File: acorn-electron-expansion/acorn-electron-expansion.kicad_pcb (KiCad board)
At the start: 2 copper layers, 100 x 100 mm, 11 parts, among them P1 Acorn Electron Expansion Conn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, P2 CONN_02X24, U1 74hct125d, U2 74LVC245 D0-7, U3 74LVC245 A0-7, U4 74LVC245 A8-15, U5 74LVC245

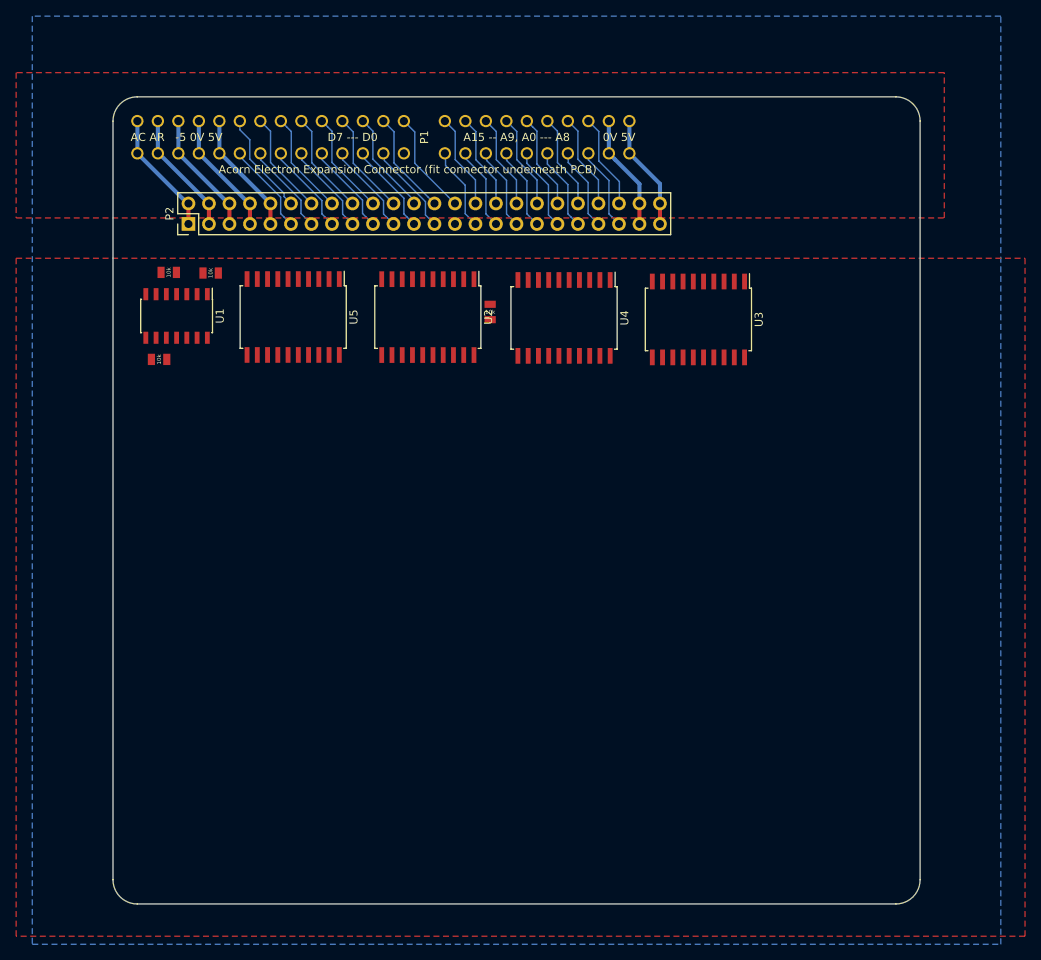
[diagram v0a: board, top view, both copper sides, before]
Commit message: Made library and module for Scarab miniSpartan6+ board, and routed most of the level conversion stuff up top
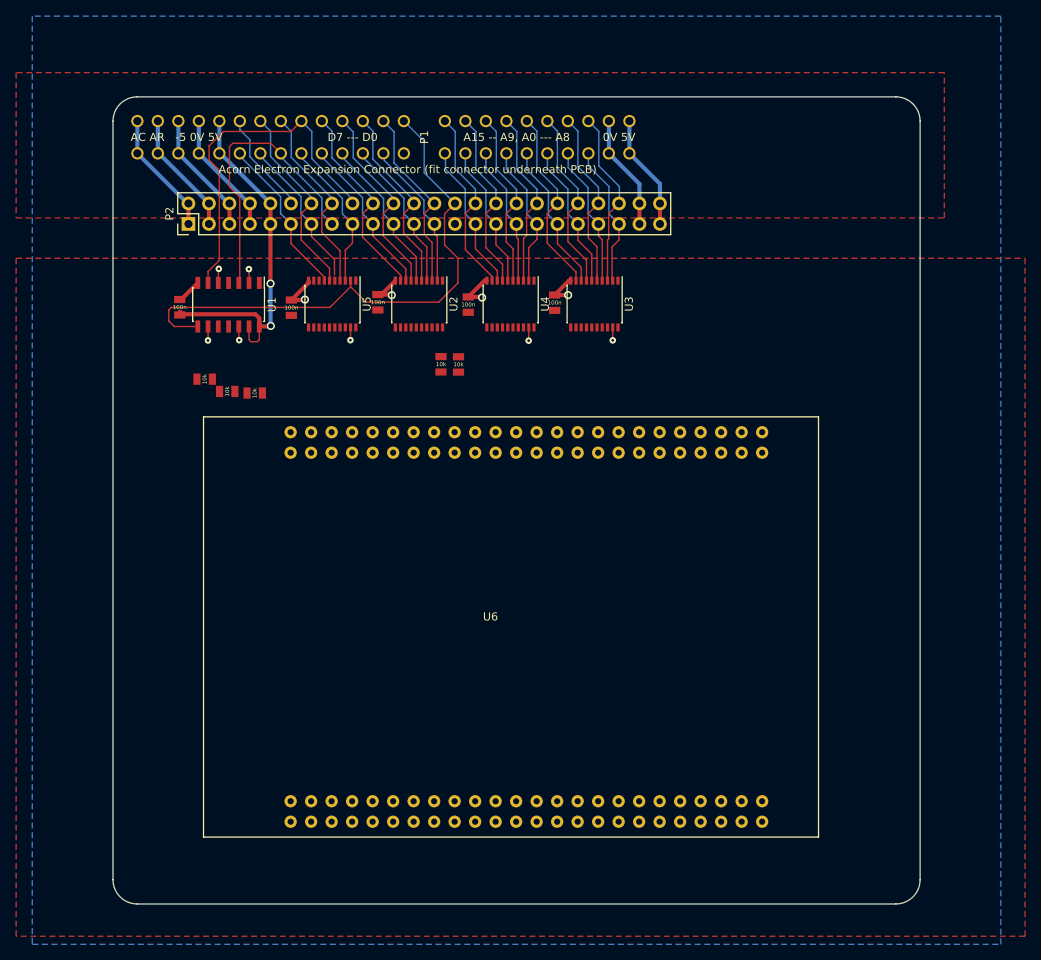
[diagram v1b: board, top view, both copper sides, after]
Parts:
- added C1: 100n, myelin-kicad:C0805_nosilkscreen, F.Cu at (108.3, 76.1)
- added C2: 100n, myelin-kicad:C0805_nosilkscreen, F.Cu at (122.1, 76.1)
- added C3: 100n, myelin-kicad:C0805_nosilkscreen, F.Cu at (132.8, 75.5)
- added C4: 100n, myelin-kicad:C0805_nosilkscreen, F.Cu at (144.0, 75.7)
- added C5: 100n, myelin-kicad:C0805_nosilkscreen, F.Cu at (154.7, 75.5)
- added R5: 10k, myelin-kicad:R0805_nosilkscreen, F.Cu at (140.6, 83.1)
- added U6: scarab_mini_spartan_6_lx25, myelin-kicad:scarab_mini_spartan_6_lx25, F.Cu at (111.2, 141.1)
- U2, U3, U4, U5: footprint Housings_SOIC:SOIC-20W_7.5x12.8mm_Pitch1.27mm -> Housings_SSOP:SSOP-20_4.4x6.5mm_Pitch0.65mm
- moved R1 15.8 mm to (117.6, 86.7)
- moved R2 14.0 mm to (111.4, 85.0)
- moved U3 13.0 mm to (159.6, 75.7)
- moved R3 9.33 mm to (114.2, 86.5)
- moved R4 7.59 mm to (142.8, 83.2)
- moved U4 6.86 mm to (149.2, 75.7)
- moved U1 6.59 mm to (114.3, 75.8)
- moved U5 5.10 mm to (127.2, 75.7)
- moved U2 1.96 mm to (137.9, 75.7)
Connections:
- U1 pad 13: Net-(U1-Pad13) -> /5V
- U2 pad 19: /GND -> /DATA_nOE
- U5 pad 13: /nRDY_3V -> /16MHZ_3V
- U5 pad 14: /16MHZ_3V -> /PHI0_3V
- U5 pad 15: /PHI0_3V -> /nRST_3V
- U5 pad 16: /nRST_3V -> /16MHZ_DIV13_3V
- U5 pad 17: /16MHZ_DIV13_3V -> /RnW_3V
- U5 pad 18: /RnW_3V -> /nRDY_3V
- U5 pad 2: /RnW -> /nRDY
- U5 pad 3: /16MHZ_DIV13 -> /RnW
- U5 pad 4: /nRST -> /16MHZ_DIV13
- U5 pad 6: /16MHZ -> /nRST
- U5 pad 7: /nRDY -> /16MHZ
- U5 pad 8: Net-(U5-Pad8) -> /GND
- U5 pad 9: Net-(U5-Pad9) -> /GND
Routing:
- net /nRDY: track 12.8 -> 68.6 mm
- net /GND: track 29.8 -> 64.0 mm, vias 0 -> 11
- net /nIRQ: track 12.8 -> 43.6 mm
- net /5V: track 29.8 -> 59.8 mm, vias 0 -> 2
- net /nNMI: track 11.4 -> 36.3 mm
- net /D7: track 12.8 -> 25.0 mm
- net /nRST: track 12.8 -> 24.5 mm
- net /D5: track 12.8 -> 24.4 mm
- net /A1: track 11.8 -> 23.3 mm
- net /A15: track 11.8 -> 23.2 mm
- net /16MHZ_DIV13: track 12.8 -> 23.9 mm
- net /D3: track 12.8 -> 23.9 mm
- net /A3: track 11.8 -> 22.8 mm
- net /A13: track 11.8 -> 22.7 mm
- net /D1: track 12.8 -> 23.4 mm
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
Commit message: Possibly final board... needs verification but almost ready to go to fab
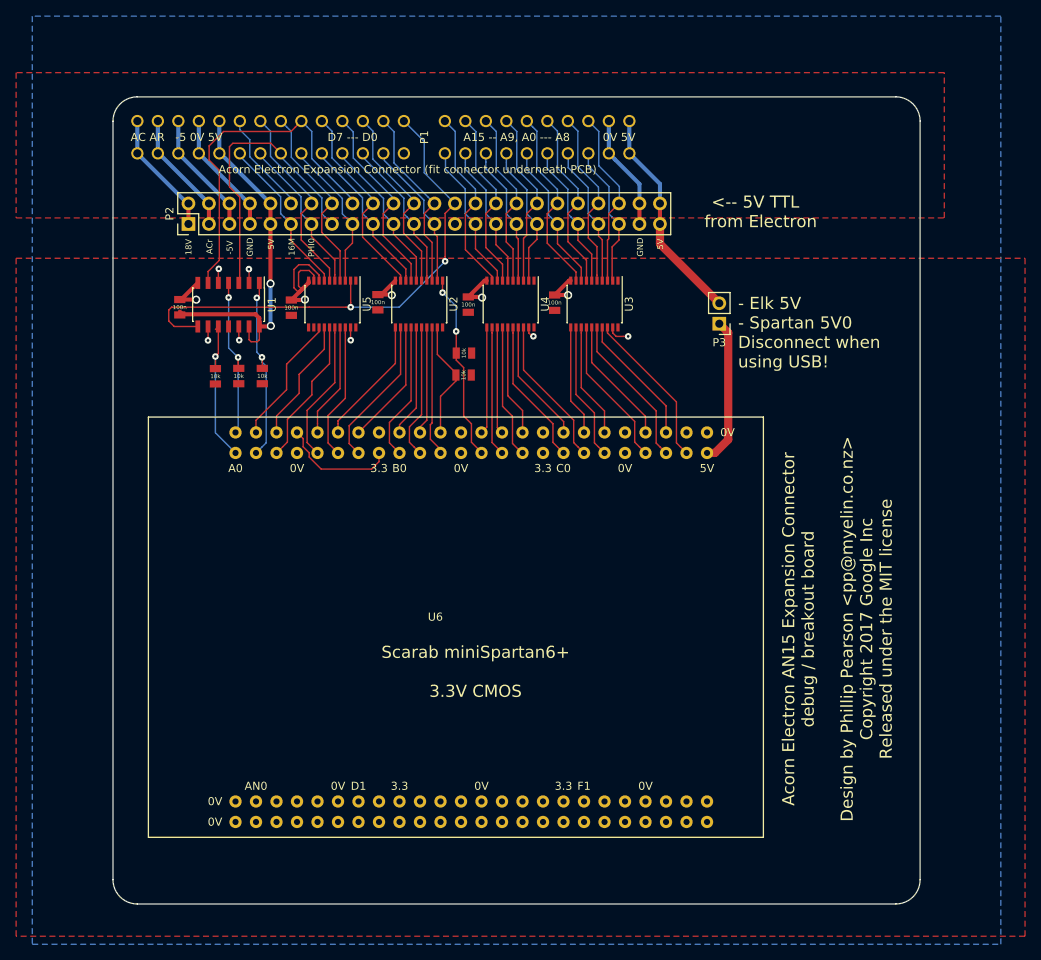
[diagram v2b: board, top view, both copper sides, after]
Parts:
- added P3: 5V / 5V0, Pin_Headers:Pin_Header_Straight_1x02_Pitch2.54mm, F.Cu at (175.1, 78.1)
- moved U6 6.83 mm to (104.4, 141.1)
- moved R2 4.24 mm to (115.6, 84.6), turned to 90 degrees
- moved R5 3.11 mm to (143.4, 84.5), turned to 180 degrees
- moved R3 2.38 mm to (112.7, 84.6), turned to 270 degrees
- moved R1 2.31 mm to (118.5, 84.6), turned to 90 degrees
- moved R4 1.56 mm to (143.5, 81.8), turned to 180 degrees
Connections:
- U6 pad A0: Net-(U6-PadA0) -> /nASSERT_nRDY
- U6 pad A1: (no net) -> /nASSERT_nIRQ
- U6 pad A10: Net-(U6-PadA10) -> /D6_3V
- U6 pad A11: Net-(U6-PadA11) -> /D5_3V
- U6 pad A2: Net-(U6-PadA2) -> /nASSERT_nNMI
- U6 pad A3: Net-(U6-PadA3) -> /16MHZ_3V
- U6 pad A4: Net-(U6-PadA4) -> /nRST_3V
- U6 pad A5: Net-(U6-PadA5) -> /PHI0_3V
- U6 pad A6: Net-(U6-PadA6) -> /16MHZ_DIV13_3V
- U6 pad A7: Net-(U6-PadA7) -> /RnW_3V
- U6 pad A8: Net-(U6-PadA8) -> /nRDY_3V
- U6 pad A9: Net-(U6-PadA9) -> /D7_3V
- U6 pad B0: Net-(U6-PadB0) -> /D4_3V
- U6 pad B1: Net-(U6-PadB1) -> /D3_3V
- U6 pad B10: Net-(U6-PadB10) -> /A12_3V
- U6 pad B11: Net-(U6-PadB11) -> /A11_3V
- U6 pad B2: Net-(U6-PadB2) -> /D2_3V
- U6 pad B3: Net-(U6-PadB3) -> /D1_3V
- U6 pad B4: Net-(U6-PadB4) -> /D0_3V
- U6 pad B5: Net-(U6-PadB5) -> /DATA_nOE
- U6 pad B6: Net-(U6-PadB6) -> /DATA_READ
- U6 pad B7: Net-(U6-PadB7) -> /A15_3V
- U6 pad B8: Net-(U6-PadB8) -> /A14_3V
- U6 pad B9: Net-(U6-PadB9) -> /A13_3V
- U6 pad C0: Net-(U6-PadC0) -> /A10_3V
- U6 pad C1: (no net) -> /A9_3V
- U6 pad C10: Net-(U6-PadC10) -> /A8_3V
- U6 pad C2: Net-(U6-PadC2) -> /A0_3V
- U6 pad C3: Net-(U6-PadC3) -> /A1_3V
- U6 pad C4: Net-(U6-PadC4) -> /A2_3V
- U6 pad C5: Net-(U6-PadC5) -> /A3_3V
- U6 pad C6: Net-(U6-PadC6) -> /A4_3V
- U6 pad C7: Net-(U6-PadC7) -> /A5_3V
- U6 pad C8: Net-(U6-PadC8) -> /A6_3V
- U6 pad C9: Net-(U6-PadC9) -> /A7_3V
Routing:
- net /nASSERT_nNMI: track 0.00 -> 23.6 mm, vias 0 -> 2
- net /DATA_READ: track 0.00 -> 23.4 mm, vias 0 -> 2
- net /nASSERT_nIRQ: track 0.00 -> 20.5 mm, vias 0 -> 2
- net /A8_3V: track 0.00 -> 19.6 mm
- net /A6_3V: track 0.00 -> 19.1 mm
- net /nASSERT_nRDY: track 0.00 -> 18.9 mm, vias 0 -> 1
- net /D6_3V: track 0.00 -> 18.7 mm
- net /A0_3V: track 0.00 -> 18.7 mm
- net /A4_3V: track 0.00 -> 18.6 mm
- net /nRST_3V: track 0.00 -> 18.3 mm
- net /A10_3V: track 0.00 -> 18.1 mm
- net /5V_scarab: track 0.00 -> 18.1 mm
- net /16MHZ_DIV13_3V: track 0.00 -> 17.5 mm
- net /D4_3V: track 0.00 -> 17.2 mm
- net /A2_3V: track 0.00 -> 17.0 mm
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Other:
- board text added: "- Elk 5V - Spartan 5V0 Disconnect when using USB!"
- board text added: "-5V"
- board text added: "16M"
- board text added: "18V"
- board text added: "5V"
- board text added: "<-- 5V TTL from Electron"
- board text added: "ACr"
- board text added: "Acorn Electron AN15 Expansion Connector debug / breakout board Design by Phillip Pearson <pp@myelin.co.nz> Copyright 2017 Google Inc Released under the MIT license"
- board text added: "GND"
- board text added: "PHI0"
- board text added: "Scarab miniSpartan6+ 3.3V CMOS"

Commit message: Changed text a little
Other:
- board text added: "pp@myelin.co.nz http://www.myelin.co.nz/ http://github.com/myelin"
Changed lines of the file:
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@@
     (area 45.247199 34.747199 254.752801 155.000001)
     (thickness 1.6)
-    (drawings 21)
+    (drawings 22)
     (tracks 641)
     (zones 0)
@@
   )
   (setup
-    (last_trace_width 1.016)
+    (last_trace_width 0.1778)
     (user_trace_width 0.254)
     (user_trace_width 0.508)
@@
       (net 4 /GND))
   )
+  (gr_text "pp@myelin.co.nz\n\nhttp://www.myelin.co.nz/\n\nhttp://github.com/myelin" (at 151.31 113.69) (layer B.SilkS)
+    (effects (font (size 2 2) (thickness 0.3)) (justify mirror))
+  )
   (gr_text 5V (at 167.82 68.24 90) (layer F.SilkS)
